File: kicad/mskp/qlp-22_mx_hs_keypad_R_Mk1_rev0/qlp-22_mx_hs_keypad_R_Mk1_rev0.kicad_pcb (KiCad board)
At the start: 2 copper layers, 162 x 112 mm, 23 parts, among them J1 Conn_01x12_Socket, SW1 Switch, SW10 Switch, SW11 Switch, SW2 Switch, SW3 Switch, SW4 Switch, SW5 Switch, SW6 Switch, SW7 Switch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

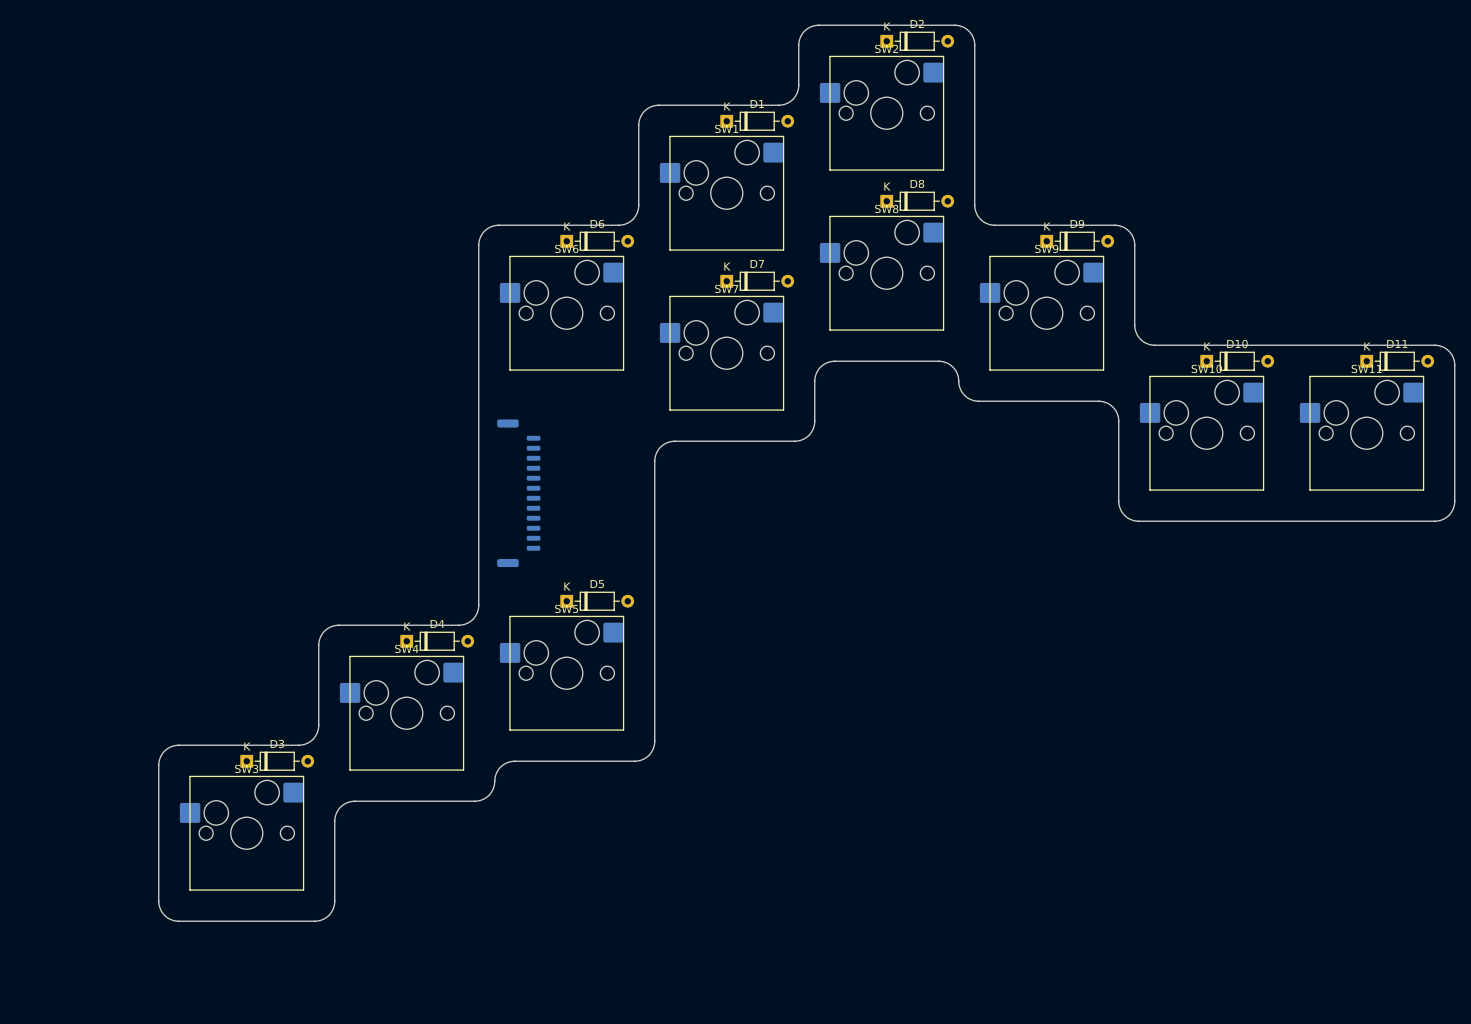
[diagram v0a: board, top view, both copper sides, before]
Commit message: Adds wiring for qlp-22_mx_hs_keypad_R_Mk1_rev0
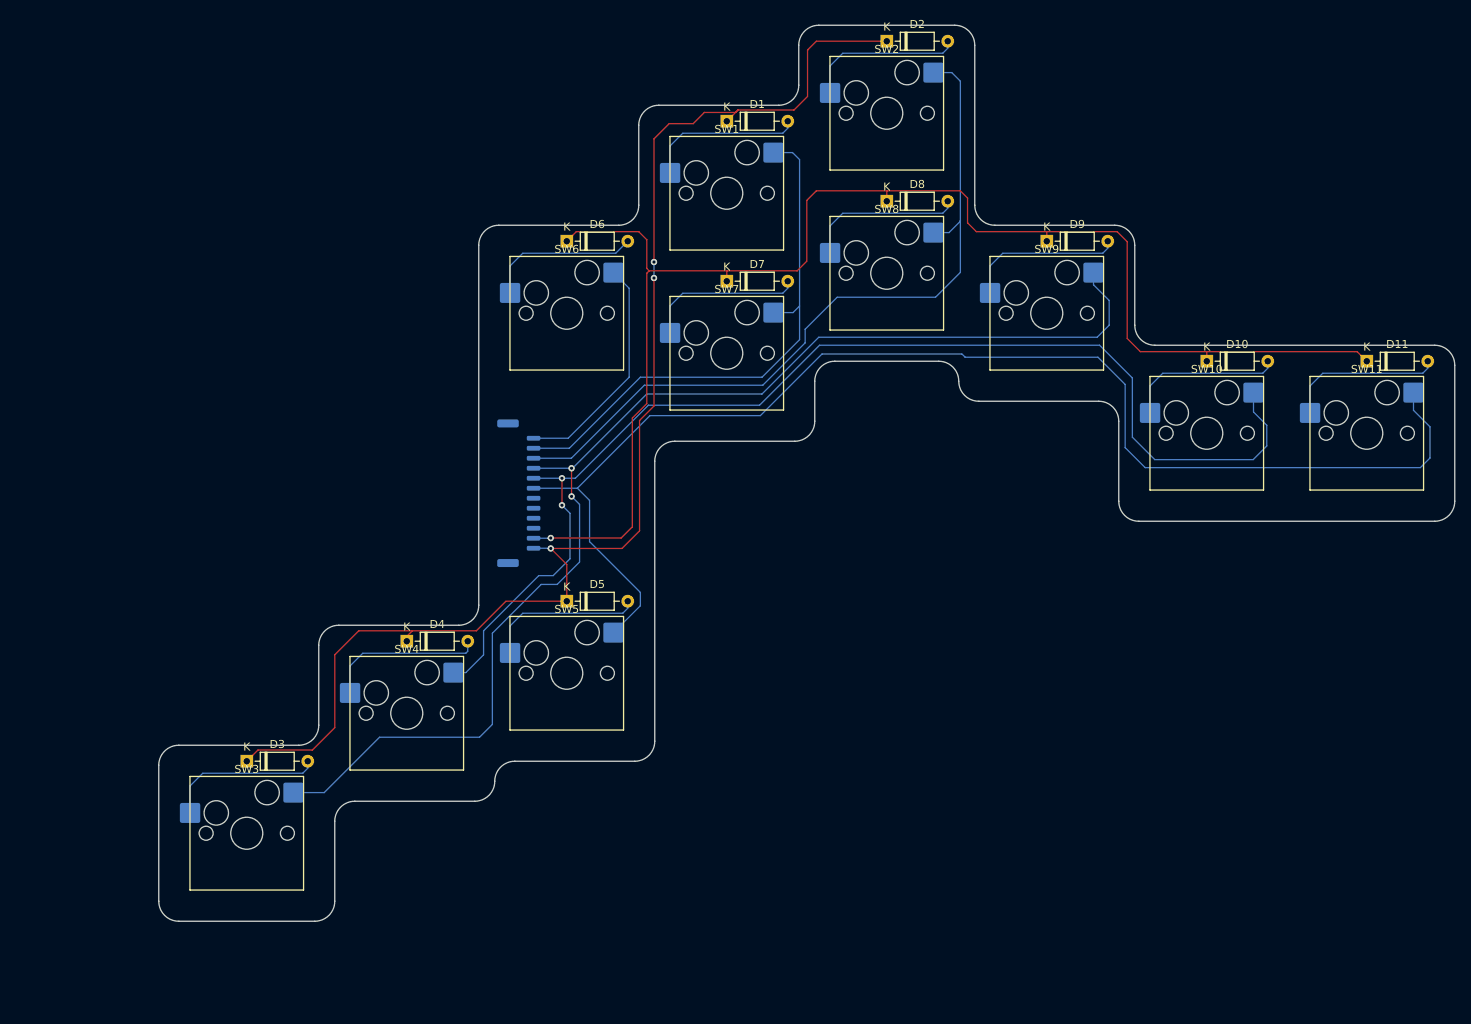
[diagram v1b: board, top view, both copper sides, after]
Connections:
- SW1 pad 2: Net-(J1-Pin_8) -> Net-(J1-Pin_11)
- SW10 pad 2: Net-(J1-Pin_11) -> Net-(J1-Pin_8)
- SW11 pad 2: Net-(J1-Pin_12) -> Net-(J1-Pin_7)
- SW2 pad 2: Net-(J1-Pin_9) -> Net-(J1-Pin_10)
- SW3 pad 2: Net-(J1-Pin_10) -> Net-(J1-Pin_9)
- SW4 pad 2: Net-(J1-Pin_11) -> Net-(J1-Pin_8)
- SW5 pad 2: Net-(J1-Pin_12) -> Net-(J1-Pin_7)
- SW6 pad 2: Net-(J1-Pin_7) -> Net-(J1-Pin_12)
- SW7 pad 2: Net-(J1-Pin_8) -> Net-(J1-Pin_11)
- SW8 pad 2: Net-(J1-Pin_9) -> Net-(J1-Pin_10)
- SW9 pad 2: Net-(J1-Pin_10) -> Net-(J1-Pin_9)
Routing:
- net Net-(D10-K): track 0.00 -> 181.8 mm, vias 0 -> 1
- net Net-(D1-K): track 0.00 -> 166.1 mm, vias 0 -> 3
- net Net-(J1-Pin_7): track 0.00 -> 161.7 mm
- net Net-(J1-Pin_9): track 0.00 -> 153.3 mm, vias 0 -> 2
- net Net-(J1-Pin_8): track 0.00 -> 149.6 mm, vias 0 -> 2
- net Net-(J1-Pin_10): track 0.00 -> 95.7 mm
- net Net-(J1-Pin_11): track 0.00 -> 68.6 mm
- net Net-(J1-Pin_12): track 0.00 -> 29.0 mm
- net Net-(D4-A): track 0.00 -> 20.1 mm
- net Net-(D8-A): track 0.00 -> 19.9 mm
- net Net-(D2-A): track 0.00 -> 19.9 mm
- net Net-(D1-A): track 0.00 -> 19.9 mm
- net Net-(D9-A): track 0.00 -> 19.9 mm
- net Net-(D7-A): track 0.00 -> 19.9 mm
- net Net-(D3-A): track 0.00 -> 19.9 mm
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
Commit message: Adds logo and OSH symbol to all mskp silkscreens
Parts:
- added G***: LOGO, Desktop:OSH_test, F.Cu at (124.9, 85.3)
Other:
- board text added: "햄"
- board text added: "햄룬드 제조"

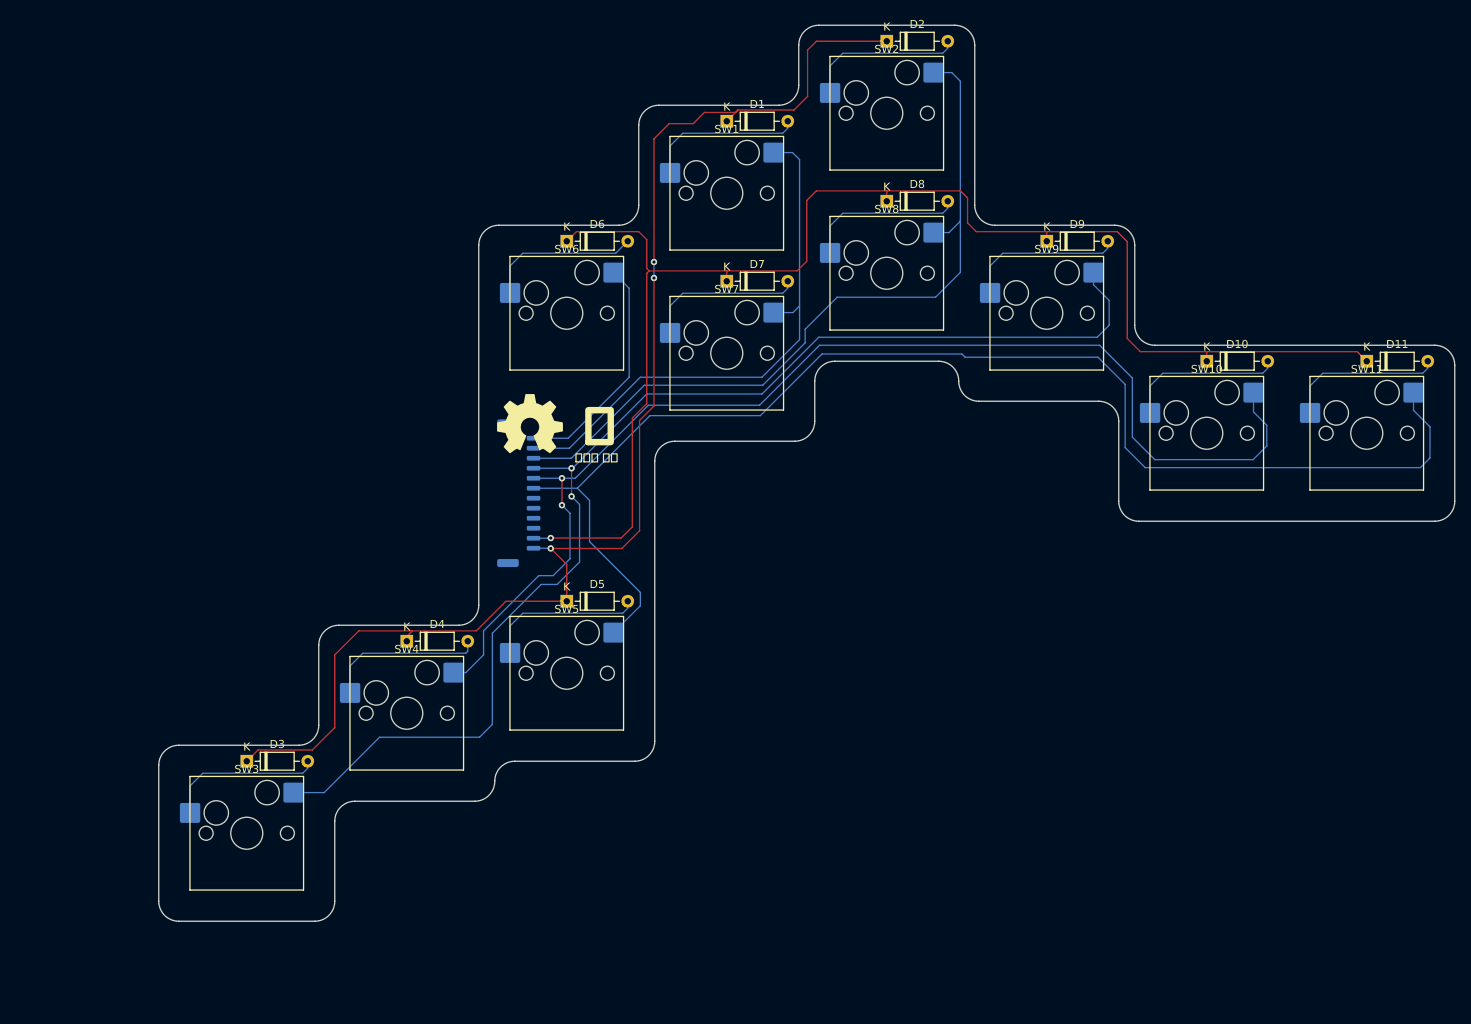
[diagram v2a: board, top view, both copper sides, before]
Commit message: Adds mounting holes to qlp-22_mx_hs_keypad_R_Mk1_rev0
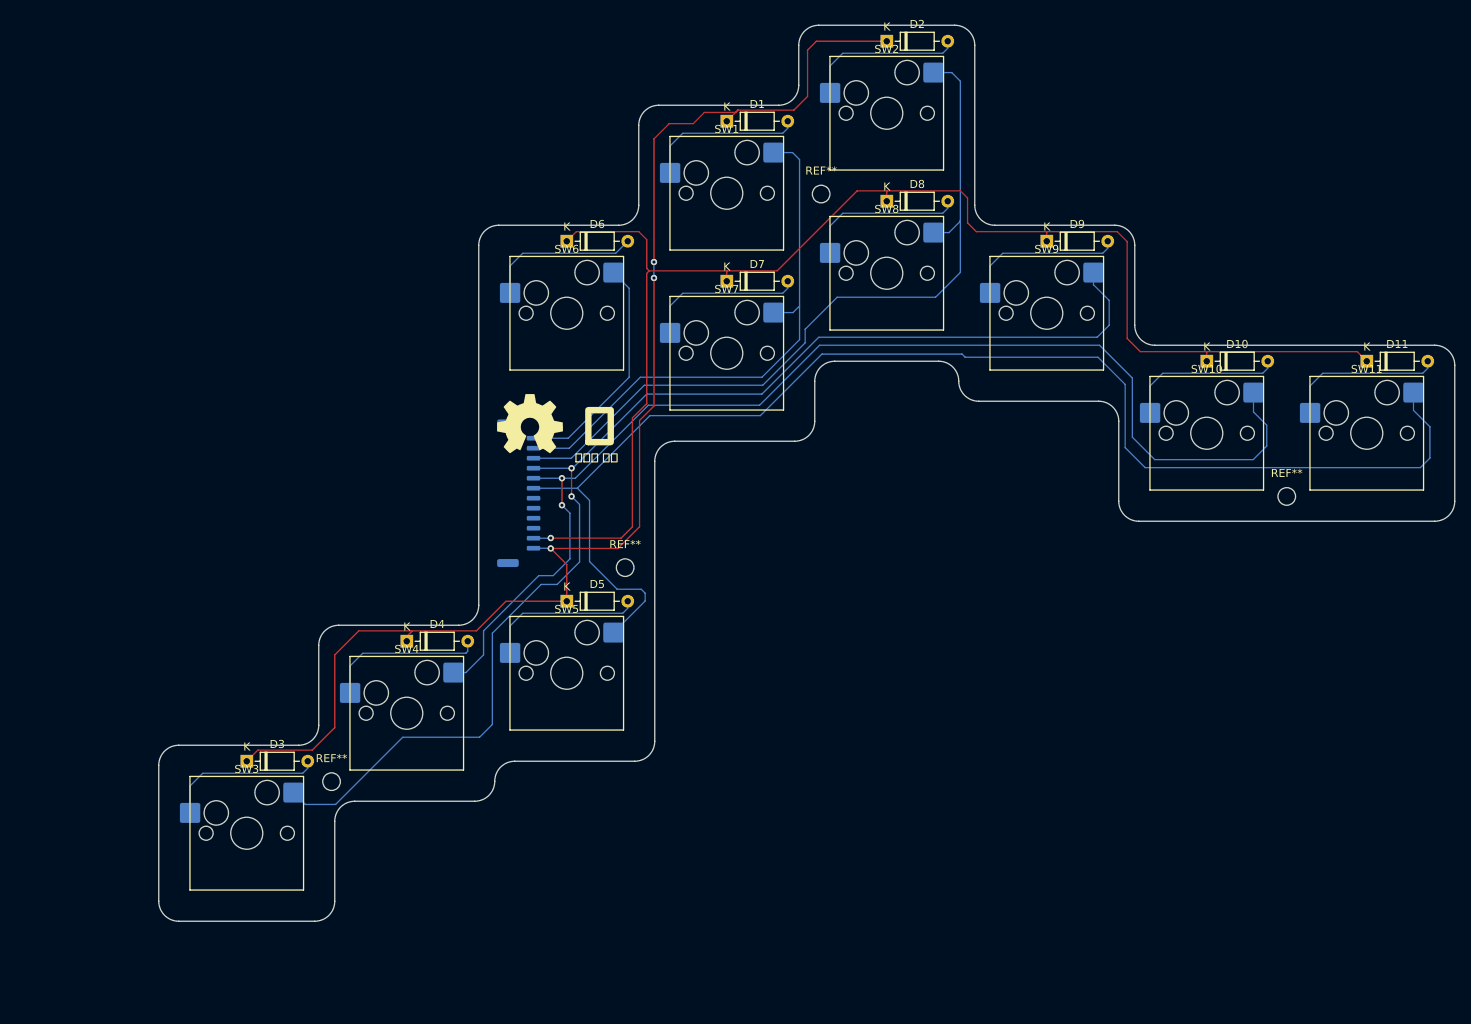
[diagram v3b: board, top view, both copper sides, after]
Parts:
- added REF**: MountingHole_2.2mm_M2_ISO14580, MountingHole:MountingHole_2.2mm_M2_ISO14580, F.Cu at (219.5, 94.4)
- added REF**: MountingHole_2.2mm_M2_ISO14580, MountingHole:MountingHole_2.2mm_M2_ISO14580, F.Cu at (161.3, 56.6)
- added REF**: MountingHole_2.2mm_M2_ISO14580, MountingHole:MountingHole_2.2mm_M2_ISO14580, F.Cu at (136.8, 103.3)
- added REF**: MountingHole_2.2mm_M2_ISO14580, MountingHole:MountingHole_2.2mm_M2_ISO14580, F.Cu at (100.1, 130.1)
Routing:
- net Net-(D10-K): track 181.8 -> 177.3 mm
- net Net-(J1-Pin_7): track 161.7 -> 164.0 mm
- net Net-(J1-Pin_9): track 153.3 -> 154.5 mm

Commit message: Finalizes mskp pcbs before first run
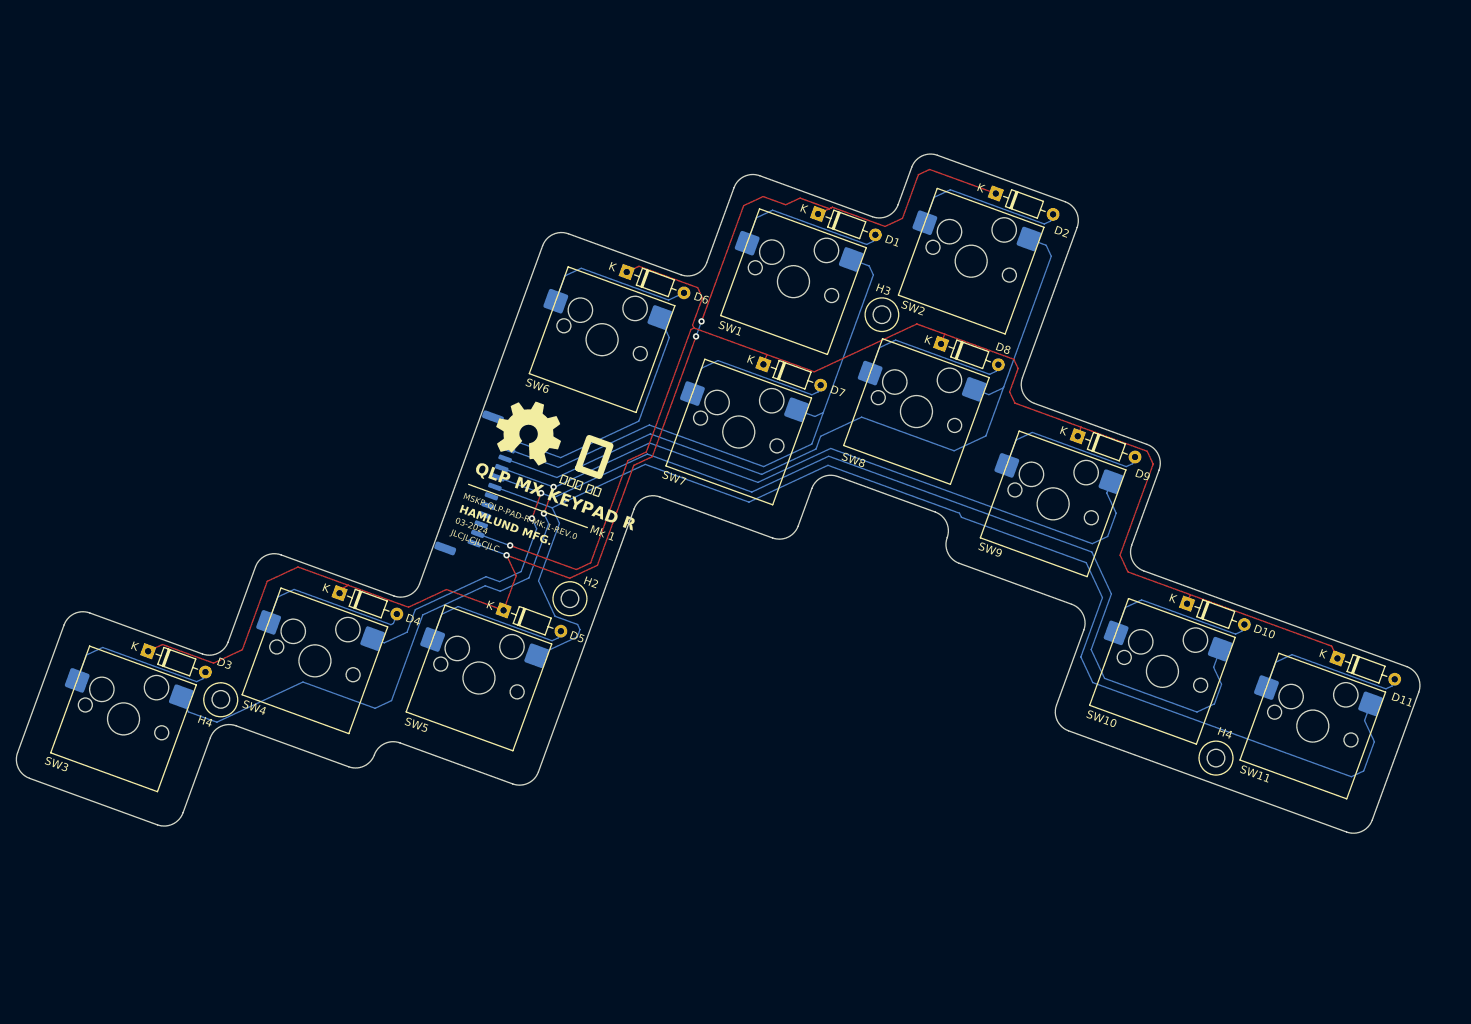
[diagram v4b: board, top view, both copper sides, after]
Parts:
- moved D11 37.3 mm to (225.8, 114.6), turned to -20 degrees
- moved SW11 37.2 mm to (222.8, 123.1), turned to -20 degrees
- moved H4 33.9 mm to (210.7, 127.1), turned to -20 degrees
- moved D10 30.4 mm to (207.0, 107.8), turned to -20 degrees
- moved SW10 30.3 mm to (204.0, 116.3), turned to -20 degrees
- moved D9 24.7 mm to (193.4, 86.9), turned to -20 degrees
- moved SW9 23.8 mm to (190.3, 95.3), turned to -20 degrees
- moved D2 23.4 mm to (183.1, 56.5), turned to -20 degrees
- moved SW2 21.3 mm to (180.1, 65.0), turned to -20 degrees
- moved SW3 21.0 mm to (74.1, 122.2), turned to -20 degrees
- moved D8 19.1 mm to (176.3, 75.3), turned to -20 degrees
- moved D3 18.5 mm to (77.2, 113.7), turned to -20 degrees
- moved SW8 17.7 mm to (173.2, 83.8), turned to -20 degrees
- moved H4 17.2 mm to (86.3, 119.8), turned to -20 degrees
- moved H3 16.9 mm to (168.9, 71.7), turned to -20 degrees
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- renumbered REF** to H2, REF** to H3, REF** to H4
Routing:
- net Net-(J1-Pin_7): track 164.0 -> 166.1 mm
- net Net-(J1-Pin_11): track 68.6 -> 70.7 mm
- net Net-(J1-Pin_10): track 95.7 -> 97.9 mm
- net Net-(J1-Pin_12): track 29.0 -> 31.1 mm
- net Net-(D1-K): track 165.8 -> 167.9 mm
- net Net-(J1-Pin_9): track 154.5 -> 156.6 mm
- net Net-(D10-K): track 177.3 -> 179.5 mm
- net Net-(J1-Pin_8): track 149.6 -> 151.7 mm
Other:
- board size 162 x 112 mm -> 175.4 x 84.9 mm
- board text added: "03-2024"
- board text added: "CONTROL MODULE"
- board text added: "HAMLUND MFG."
- board text added: "JLCJLCJLCJLC"
- board text added: "MSKP-QLP-PAD-R-MK.1-REV.0"
- board text added: "Mk 1"
- board text added: "QLP MX KEYPAD R"
- board text added: "S0:0"
- board text added: "S0:1"
- board text added: "S0:2"
- board text added: "S0:3"
- board text added: "S0:4"
- board text added: "S1:0"
- board text added: "S1:1"
- board text added: "S1:2"
- board text added: "S1:3"
- board text added: "S1:4"
- board text added: "S1:5"
